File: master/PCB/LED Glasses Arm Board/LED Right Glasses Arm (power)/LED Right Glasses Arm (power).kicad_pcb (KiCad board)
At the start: 2 copper layers, 130.8 x 20.4 mm, 24 parts, among them J1 Conn_01x02_Male, J2 Conn_01x01_Male, J3 Conn_01x01_Male, Q1 TP0610T, SW1 SW_SPST, U1 TPS63060

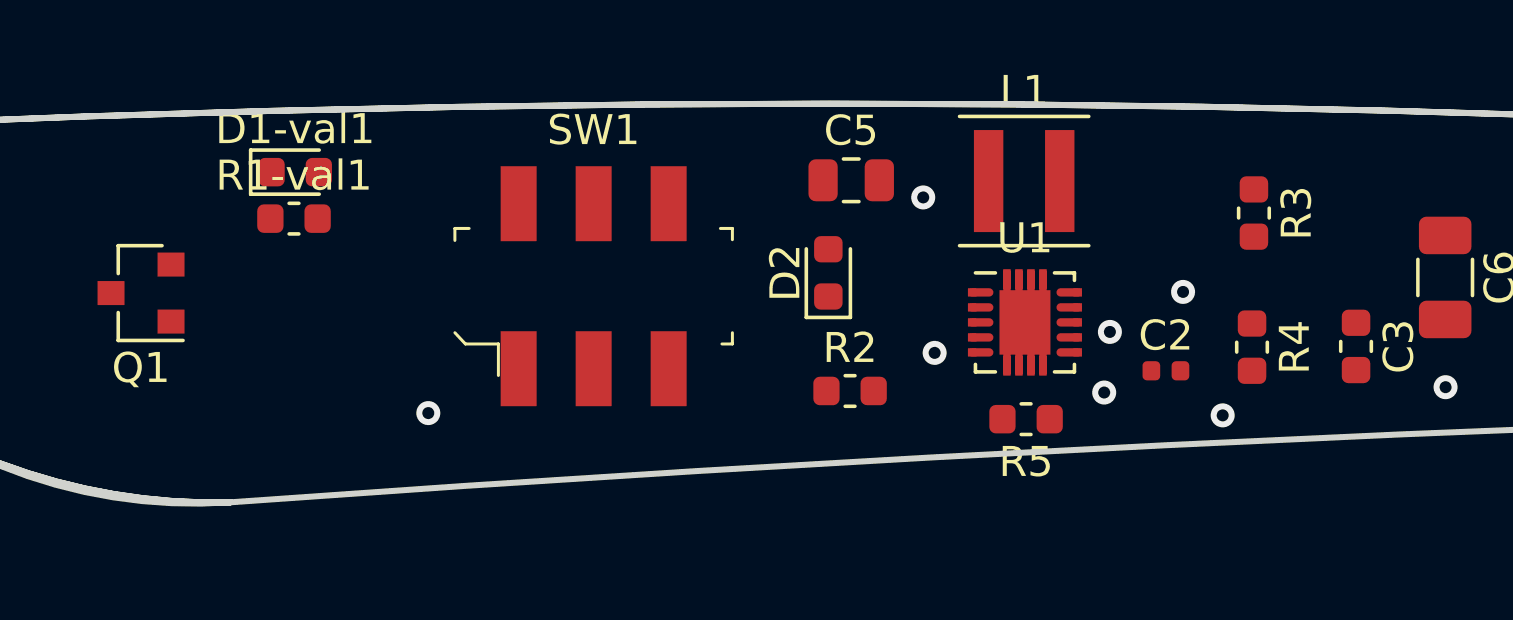
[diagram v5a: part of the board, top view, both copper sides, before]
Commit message: Updated with all components with links
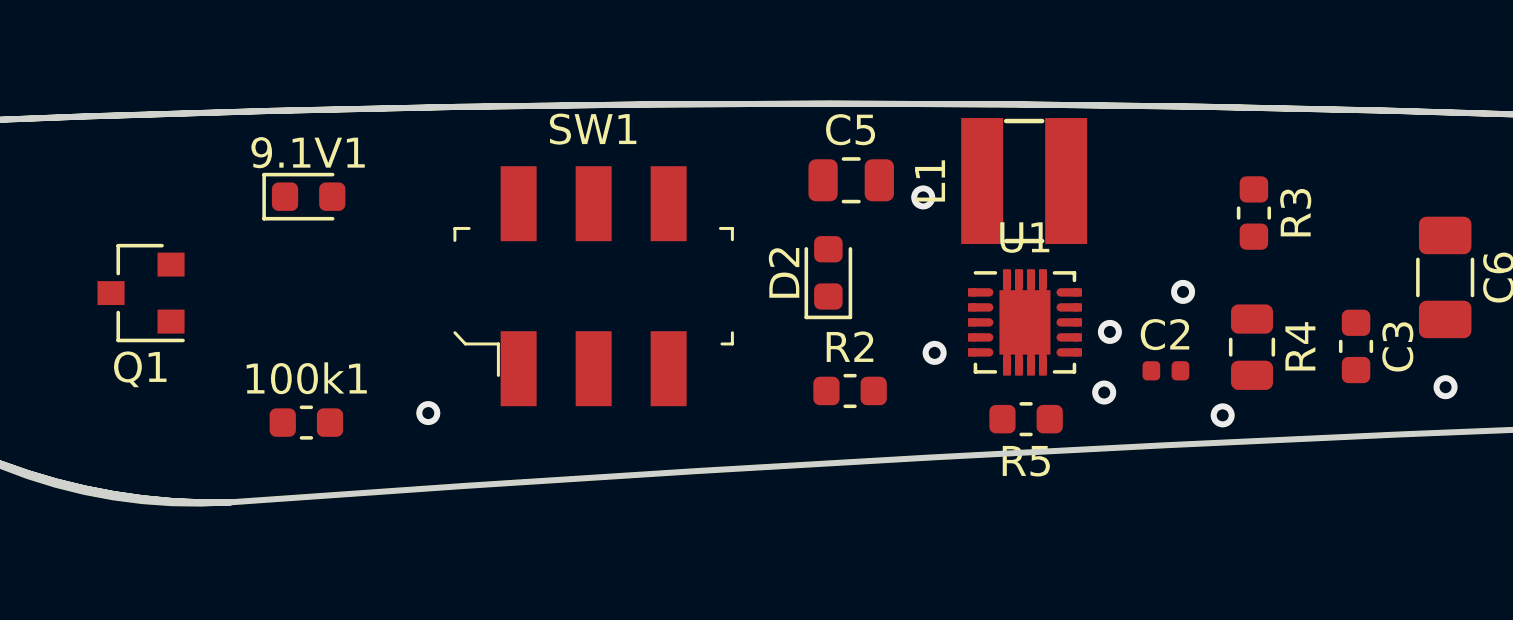
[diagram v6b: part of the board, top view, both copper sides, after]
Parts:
- removed D1-val1: D_Zener_Small, Diode_SMD:D_0603_1608Metric
- removed R1-val1: R_Small_US, Resistor_SMD:R_0603_1608Metric
- added 100k1: R_Small_US, Resistor_SMD:R_0603_1608Metric, F.Cu at (150.7, 99.5)
- added 9.1V1: D_Zener_Small, Diode_SMD:D_0603_1608Metric, F.Cu at (150.8, 92.0)
- D2: value LED -> LED Red
- D3: value LED -> LED Green
- L1: footprint Inductor_SMD:L_Coilcraft_XxL4020 -> sft:SRN4018TA
- R4: footprint Resistor_SMD:R_0603_1608Metric -> Resistor_SMD:R_0805_2012Metric
- R5: value 1MOhm -> 1M
- turned L1 to 90 degrees

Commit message: added links
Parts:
- moved 9.1V1 3.32 mm to (150.6, 95.3), turned to 270 degrees
- moved D2 0.37 mm to (168.1, 94.9)
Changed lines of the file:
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@@
   )
   (module Diode_SMD:D_0603_1608Metric (layer F.Cu)
-    (at 150.7998 91.9734)
+    (at 150.5585 95.2881 270)
     (descr "Diode SMD 0603 (1608 Metric), square (rectangular) end terminal, IPC_7351 nominal, (Body size source: http://www.tortai-tech.com/upload/download/2011102023233369053.pdf), generated with kicad-footprint-generator")
     (tags diode)
     (attr smd)
-    (fp_text reference 9.1V1 (at 0 -1.43) (layer F.SilkS)
-      (effects (font (size 1 1) (thickness 0.15)))
-    )
-    (fp_text value D_Zener_Small (at 0 1.43) (layer F.Fab)
+    (fp_text reference 9.1V1 (at 0 -1.43 270) (layer F.SilkS)
+      (effects (font (size 1 1) (thickness 0.15)))
+    )
+    (fp_text value D_Zener_Small (at 0 1.43 270) (layer F.Fab)
       (effects (font (size 1 1) (thickness 0.15)))
     )
@@
     (fp_line (start 1.48 -0.73) (end 1.48 0.73) (layer F.CrtYd) (width 0.05))
     (fp_line (start 1.48 0.73) (end -1.48 0.73) (layer F.CrtYd) (width 0.05))
-    (fp_text user %R (at 0 0) (layer F.Fab)
+    (fp_text user %R (at 0 0 270) (layer F.Fab)
       (effects (font (size 0.4 0.4) (thickness 0.06)))
     )
-    (pad 1 smd roundrect (at -0.7875 0) (size 0.875 0.95) (layers F.Cu F.Paste F.Mask) (roundrect_rratio 0.25)
+    (pad 1 smd roundrect (at -0.7875 0 270) (size 0.875 0.95) (layers F.Cu F.Paste F.Mask) (roundrect_rratio 0.25)
       (net 12 "Net-(9.1V1-Pad1)"))
-    (pad 2 smd roundrect (at 0.7875 0) (size 0.875 0.95) (layers F.Cu F.Paste F.Mask) (roundrect_rratio 0.25)
+    (pad 2 smd roundrect (at 0.7875 0 270) (size 0.875 0.95) (layers F.Cu F.Paste F.Mask) (roundrect_rratio 0.25)
       (net 13 "Net-(100k1-Pad1)"))
     (model ${KISYS3DMOD}/Diode_SMD.3dshapes/D_0603_1608Metric.wrl
@@
   )
   (module LED_SMD:LED_0603_1608Metric (layer F.Cu)
-    (at 168.1226 94.5134 90)
+    (at 168.0972 94.8817 90)
     (descr "LED SMD 0603 (1608 Metric), square (rectangular) end terminal, IPC_7351 nominal, (Body size source: http://www.tortai-tech.com/upload/download/2011102023233369053.pdf), generated with kicad-footprint-generator")
     (tags diode)

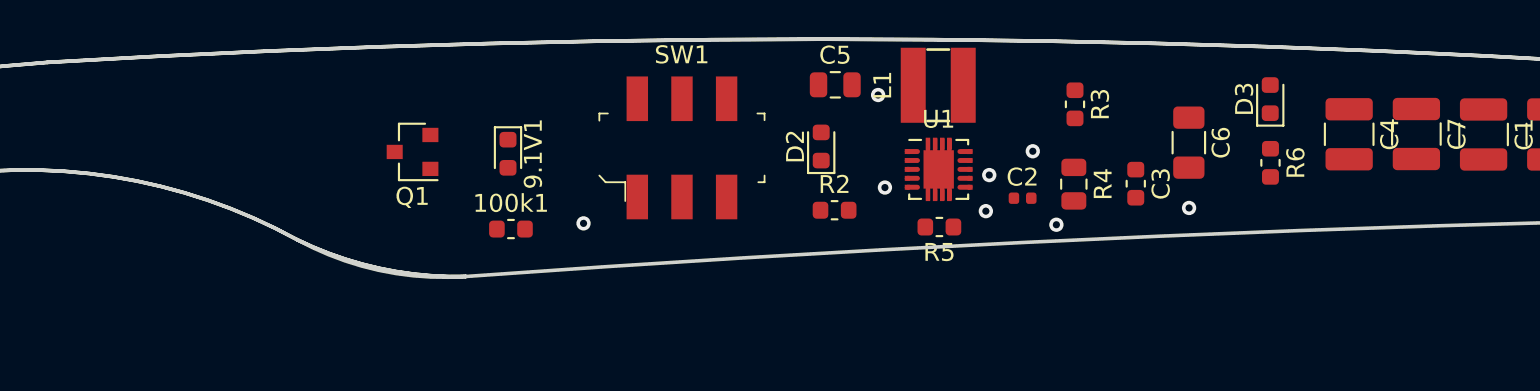
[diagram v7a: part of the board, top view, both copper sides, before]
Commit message: added labels, new zener diode, began layout
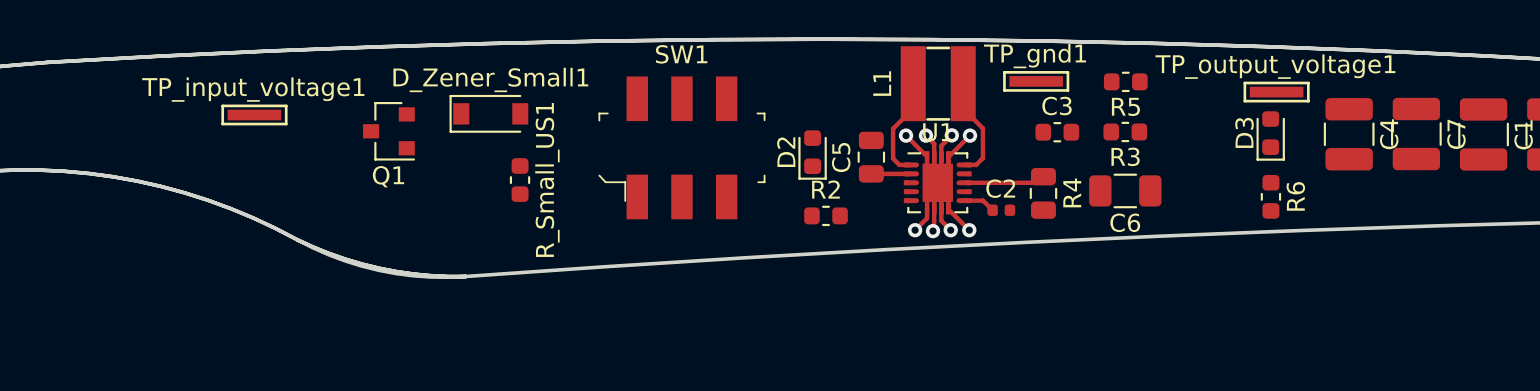
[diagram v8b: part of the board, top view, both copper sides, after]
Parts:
- removed 100k1: R_Small_US, Resistor_SMD:R_0603_1608Metric
- removed 9.1V1: D_Zener_Small, Diode_SMD:D_0603_1608Metric
- added D_Zener_Small1: 6V, Diode_SMD:D_SOD-123, F.Cu at (149.6, 93.1)
- added R_Small_US1: 100k1, Resistor_SMD:R_0603_1608Metric, F.Cu at (151.2, 96.8)
- added TP_gnd1: TestPoint, Connector_PinHeader_1.00mm:PinHeader_1x01_P1.00mm_Vertical_SMD_CUSTOM, F.Cu at (180.1, 93.3)
- added TP_input_voltage1: TestPoint, Connector_PinHeader_1.00mm:PinHeader_1x01_P1.00mm_Vertical_SMD_CUSTOM, F.Cu at (136.4, 95.1)
- added TP_output_voltage1: TestPoint, Connector_PinHeader_1.00mm:PinHeader_1x01_P1.00mm_Vertical_SMD_CUSTOM, F.Cu at (193.6, 93.9)
- U1: value TPS63060 -> TPS63061DSCT
- moved R5 13.2 mm to (185.2, 91.3)
- moved C3 5.26 mm to (181.3, 94.1), turned to 0 degrees
- moved C5 4.53 mm to (170.9, 95.5), turned to 90 degrees
- moved C6 4.47 mm to (185.1, 97.4), turned to 180 degrees
- moved R3 3.22 mm to (185.1, 94.1), turned to 180 degrees
- moved D3 1.91 mm to (193.3, 94.1)
- moved R6 1.91 mm to (193.3, 97.7)
- moved R4 1.78 mm to (180.5, 97.5)
- moved Q1 1.76 mm to (143.9, 94.0)
- moved C2 1.37 mm to (178.2, 98.5)
- moved U1 0.75 mm to (174.6, 96.9)
- moved D2 0.58 mm to (167.6, 95.2)
- moved R2 0.58 mm to (168.4, 98.8)
- moved L1 0.09 mm to (174.7, 91.4)
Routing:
- net GND: track 0.00 -> 12.3 mm, vias 6 -> 8
- net Net-(L1-Pad1): track 0.00 -> 5.84 mm
- net Net-(L1-Pad2): track 0.00 -> 5.84 mm
- net Net-(C3-Pad1): track 0.00 -> 4.58 mm, vias 2 -> 0
- net Net-(C5-Pad1): track 0.00 -> 2.25 mm
- net Net-(C2-Pad1): track 0.00 -> 1.82 mm
